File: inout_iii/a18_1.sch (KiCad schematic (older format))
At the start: 33 parts, among them U18001 74HC02, U18002 74HC04, U18003 74HC02, U18004 74HC02, U18005 74HC02, U18006 74HC27, U18007 74LVC07, U18008 74HC04, U18009 74HC02, U18010 74HC4002, U18011 74HC02, U18012 74HC02, U18013 74HC04, U18014 74HC02, U18015 74HC02, U18016 74HC02, U18017 74HC27, U18018 74HC02, U18019 74HC02, U18020 74HC04, U18021 74HC02, U18022 74HC02, U18023 74HC27, U18024 74HC02, U18025 74HC04, U18026 74HC02, U18027 74HC02, U18028 74HC4002, U18029 74HC27, U18030 74HC02, U18031 74HC04

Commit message: Added most of the rest of Inout III and tied it in. Still not sure where to put the downlink stuff, standby, and CHOR propers.
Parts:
- added U18053: 74HC04, symbol 74HC04
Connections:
- net F09A/: now also U18053.6
- net GND: now also U18053.7 (GND)
- net VCC: now also U18053.14 (VCC)
- new net F09A: U18053.5
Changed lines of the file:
@@
 $EndComp
 $Comp
-L VCC #PWR08
+L VCC #PWR06
 U 1 1 5761F17B
 P 8900 1450
-F 0 "#PWR08" H 8900 1300 50  0001 C CNN
+F 0 "#PWR06" H 8900 1300 50  0001 C CNN
 F 1 "VCC" H 8900 1600 50  0000 C CNN
 F 2 "" H 8900 1450 60  0000 C CNN
@@
 	1    0    0    -1
 $EndComp
-Text HLabel 9500 1700 0    60   Input ~ 0
-F09A/
 $Comp
 L 74HC27 U18006
@@
 $EndComp
 $Comp
-L VCC #PWR09
+L VCC #PWR07
 U 1 1 576688D1
 P 22100 1450
-F 0 "#PWR09" H 22100 1300 50  0001 C CNN
+F 0 "#PWR07" H 22100 1300 50  0001 C CNN
 F 1 "VCC" H 22100 1600 50  0000 C CNN
 F 2 "" H 22100 1450 60  0000 C CNN
@@
 	1    0    0    -1
 $EndComp
-Text HLabel 22700 1700 0    60   Input ~ 0
-F09A/
 $Comp
 L 74HC27 U18017
@@
 	1    0    0    -1
 $EndComp
-Text HLabel 21500 8550 0    60   Input ~ 0
-F09A/
 $Comp
 L 74HC27 U18029
@@
 	23700 6950 23700 3400
 Wire Wire Line
-	22750 1700 22700 1700
+	22750 1700 22450 1700
 Wire Wire Line
 	22500 1900 22750 1900
@@
 	22500 10450 22500 10250
 Wire Wire Line
-	21550 8550 21500 8550
+	21550 8550 21250 8550
 Wire Wire Line
 	21300 8750 21550 8750
@@
 Text Label 11750 8300 2    60   ~ 0
 F09D
+$Comp
+L 74HC04 U18053
+U 3 1 571E5751
+P 8600 1050
+F 0 "U18053" H 8750 1150 40  0000 C CNN
+F 1 "74HC04" H 8800 950 40  0000 C CNN
+F 2 "" H 8600 1050 60  0000 C CNN
+F 3 "" H 8600 1050 60  0000 C CNN
+	3    8600 1050
+	1    0    0    -1
+$EndComp
+Text HLabel 8100 1050 0    60   Input ~ 0
+F09A
+Wire Wire Line
+	8150 1050 8100 1050
+Wire Wire Line
+	9500 1700 9500 1050
+Wire Wire Line
+	9500 1050 9050 1050
+Text Label 9250 1050 0    60   ~ 0
+F09A/
+Text Label 22450 1700 0    60   ~ 0
+F09A/
+Text Label 21250 8550 0    60   ~ 0
+F09A/
 $EndSCHEMATC

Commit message: Lots of initial conditions, some missed gates, and some wiring fixes
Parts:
- U18002, U18008, U18020, U18025: Initial (none) -> 1
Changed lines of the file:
@@
 F 2 "" H 1500 6750 60  0000 C CNN
 F 3 "" H 1500 6750 60  0000 C CNN
+F 4 "1" H 1550 6750 60  0000 C CIN "Initial"
 	6    1500 6750
 	1    0    0    -1
@@
 F 2 "" H 14700 6750 60  0000 C CNN
 F 3 "" H 14700 6750 60  0000 C CNN
+F 4 "1" H 14750 6750 60  0000 C CIN "Initial"
 	4    14700 6750
 	1    0    0    -1
@@
 F 2 "" H 12900 11950 60  0000 C CNN
 F 3 "" H 12900 11950 60  0000 C CNN
+F 4 "1" H 12950 11950 60  0000 C CIN "Initial"
 	4    12900 11950
 	1    0    0    -1
@@
 F 2 "" H 14700 10250 60  0000 C CNN
 F 3 "" H 14700 10250 60  0000 C CNN
+F 4 "1" H 14750 10250 60  0000 C CIN "Initial"
 	1    14700 10250
 	1    0    0    -1

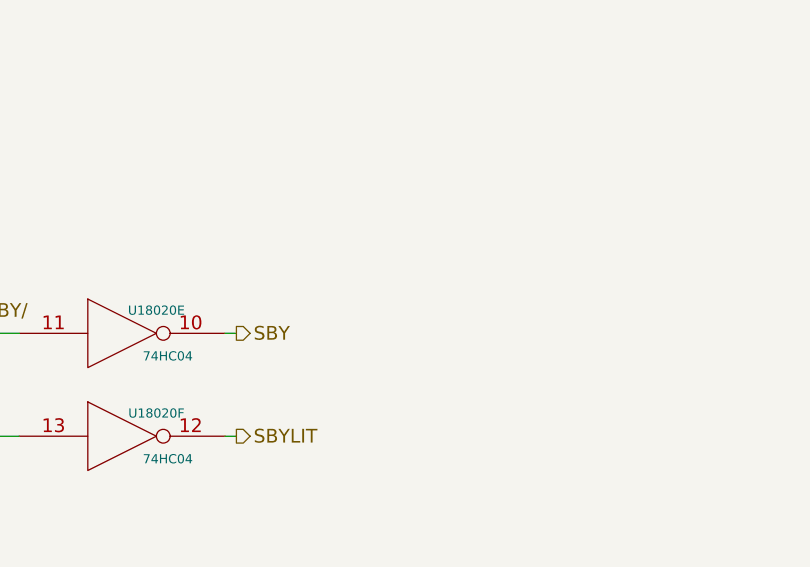
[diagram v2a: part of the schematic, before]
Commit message: Did another pass through the schematics and added in some missing gates
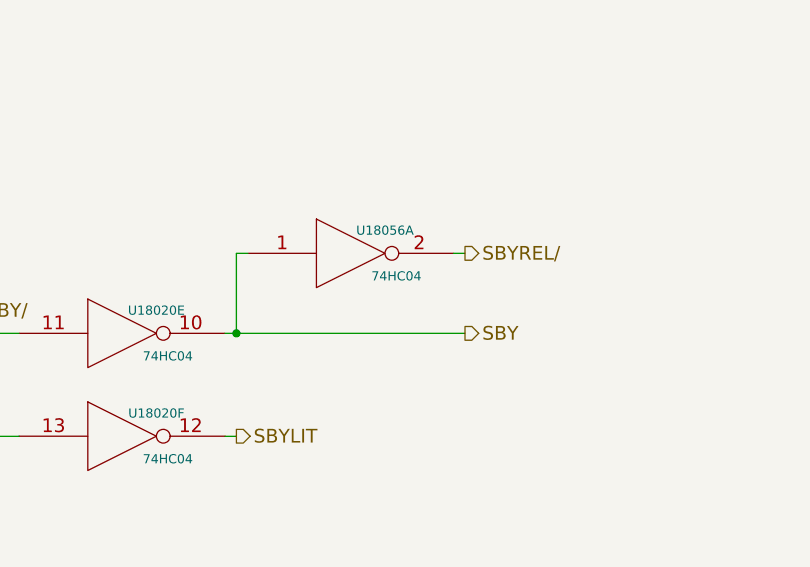
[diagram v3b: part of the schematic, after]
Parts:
- added U18056: 74HC04, symbol 74HC04
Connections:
- net GND: now also U18056.7 (GND)
- net SBY: now also U18056.1
- net VCC: now also U18056.14 (VCC)
- new net SBYREL/: U18056.2
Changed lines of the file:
@@
 Text HLabel 13450 11850 2    60   Output ~ 0
 STNDBY/
-Text HLabel 14800 11950 2    60   Output ~ 0
+Text HLabel 15800 11950 2    60   Output ~ 0
 SBY
 $Comp
@@
 Connection ~ 13400 11950
 Wire Wire Line
-	14800 11950 14750 11950
+	15800 11950 14750 11950
 Wire Wire Line
 	12350 11950 12350 12300
@@
 Text Label 21250 8550 0    60   ~ 0
 F09A/
+$Comp
+L 74HC04 U18056
+U 1 1 5721E8D2
+P 15300 11600
+F 0 "U18056" H 15450 11700 40  0000 C CNN
+F 1 "74HC04" H 15500 11500 40  0000 C CNN
+F 2 "" H 15300 11600 60  0000 C CNN
+F 3 "" H 15300 11600 60  0000 C CNN
+	1    15300 11600
+	1    0    0    -1
+$EndComp
+Wire Wire Line
+	14850 11600 14800 11600
+Wire Wire Line
+	14800 11600 14800 11950
+Connection ~ 14800 11950
+Wire Wire Line
+	15750 11600 15800 11600
+Text HLabel 15800 11600 2    60   Output ~ 0
+SBYREL/
 $EndSCHEMATC

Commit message: Fixed not->1-input nor in the rest of the modules.
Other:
- moved on the sheet: R18001, R18002, U18001A, U18001B, U18001C, U18001D, U18002A, U18002B, U18002C, U18002D, U18002E, U18002F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

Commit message: Updated Inout III for the new power nets. Conveniently, only the standby-controlling stuff is on standby power
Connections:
- net labels added: +4VSW
- net labels removed: VCC
